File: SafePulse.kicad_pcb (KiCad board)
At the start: 13 copper layers, 40.6 x 20.8 mm, 88 parts, among them IC1 S-35770E01I-K8T2U, J1 Conn_01x03_Male, J2 4208, Q1 FQT7N10L, Q2 BC846A, Q3 MMBT3906, Q4 MMBT3906, U1 TS4061AICT-1.25, U2 74HC14, U3 TLV27L1DBVT, U33 MAX9910EXK+T, U4 CD14538BM

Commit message: Updated production files
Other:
- copper layers 13 -> 4

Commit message: cleaned up files
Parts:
- removed REF**: LOGO, Library:QR_code_SafePulse
- removed U3: TLV27L1DBVT, Package_TO_SOT_SMD:SOT-23-5
- Q2: footprint Package_TO_SOT_SMD:SOT-323_SC-70_Handsoldering -> Package_TO_SOT_SMD:SOT-323_SC-70
- moved C4 2.00 mm to (134.2, 72.9), turned to 180 degrees
- moved H1 1.04 mm to (138.7, 73.0)
- moved C27 0.89 mm to (138.7, 70.2)
- moved R18 0.36 mm to (142.1, 72.7)
- moved R4 0.25 mm to (136.9, 67.7)
- moved C1 0.24 mm to (138.9, 67.7)
- moved C19 0.22 mm to (137.9, 70.4)
- turned U33 to -90 degrees
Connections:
- IC1 pad 7: /SDA -> Net-(IC1-SCL)
- J1 pad 4: Net-(IC1-SDA) -> Net-(IC1-SCL)
- J1 pad 5: /SDA -> Net-(IC1-SDA)
- J2 pad 4: /SDA -> Net-(IC1-SCL)
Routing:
- net /SDA: track 19.7 -> 0.00 mm, vias 2 -> 0
- net Net-(IC1-SCL): track 0.00 -> 16.2 mm, vias 0 -> 2
- net Net-(U33--): track 23.9 -> 15.4 mm
- net Net-(U33-V+): track 21.1 -> 13.1 mm
- net GND: track 64.6 -> 59.6 mm, vias 14 -> 13
- net Net-(U33-+): track 10.0 -> 5.26 mm
- net Net-(R3-Pad2): track 8.62 -> 5.09 mm
- net Net-(C1-Pad1): track 10.2 -> 6.91 mm
- net +3V3: track 51.3 -> 48.2 mm
- net Net-(IC1-SDA): track 18.7 -> 20.3 mm
- net Net-(H1-Pad1): track 5.48 -> 4.25 mm
- net Net-(J1-Pin_1): track 4.55 -> 3.82 mm
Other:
- board text added: "SCL"
- board text added: "SDA"

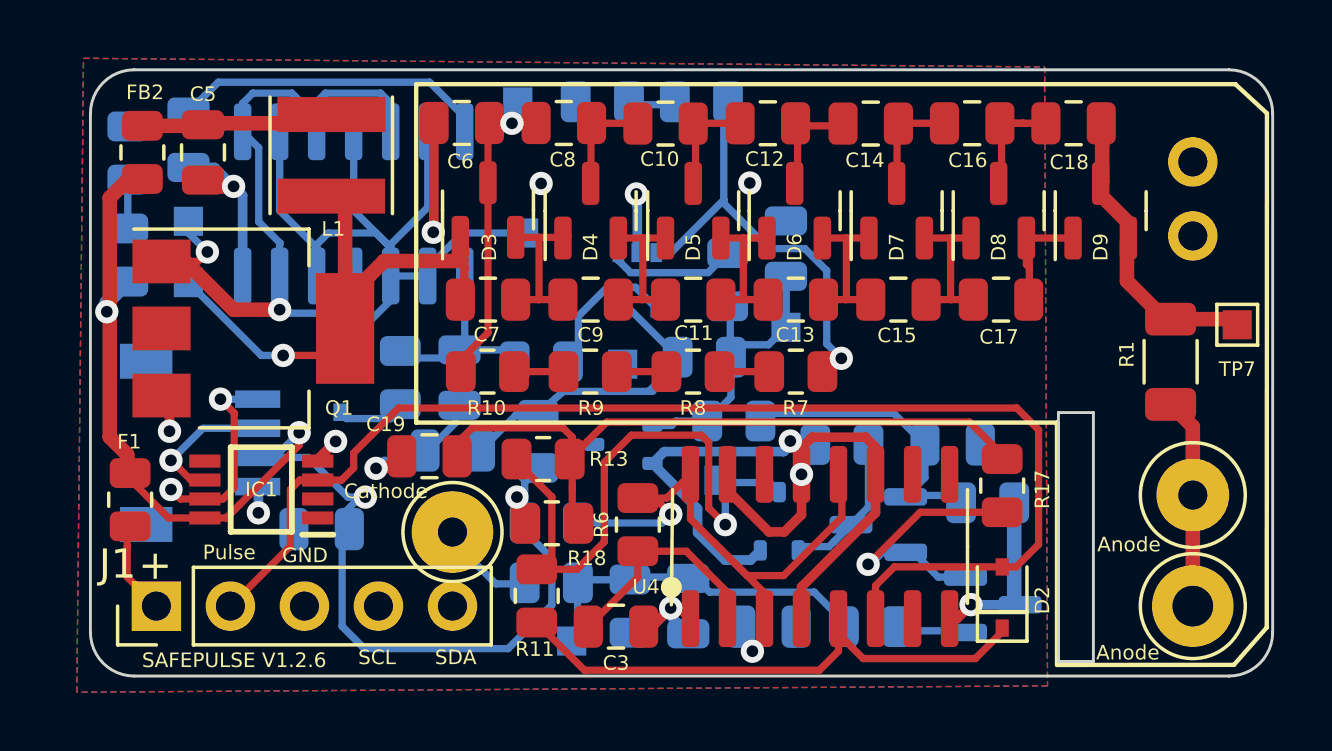
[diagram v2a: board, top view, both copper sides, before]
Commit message: Added QR code and updated files from Allan
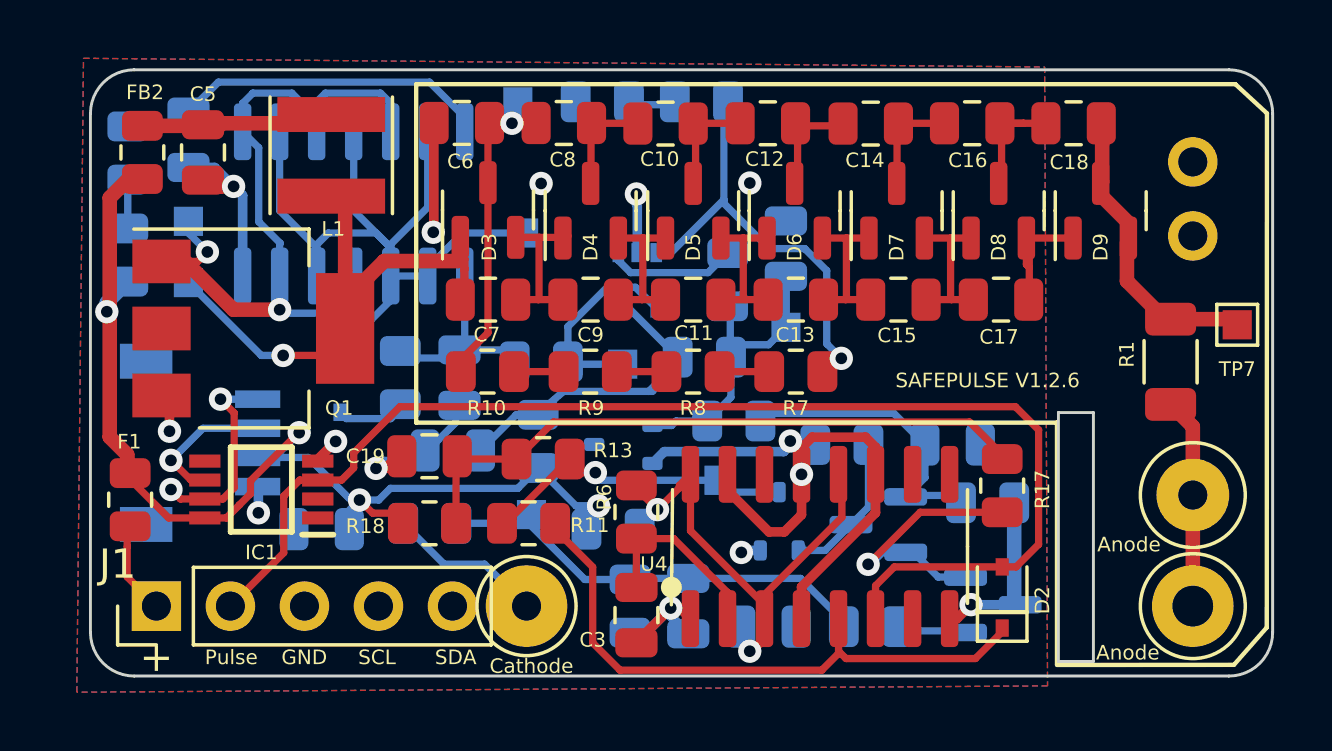
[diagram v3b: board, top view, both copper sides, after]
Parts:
- added REF**: LOGO, Library:QR_code_SafePulse, F.Cu at (156.3, 63.6)
- moved R21 4.64 mm to (137.9, 72.7)
- moved TP8 4.55 mm to (141.4, 72.4)
- moved R18 4.20 mm to (137.9, 72.7)
- moved H1 3.59 mm to (141.2, 75.6)
- moved R11 2.51 mm to (141.3, 72.7), turned to 180 degrees
- moved R12 2.13 mm to (144.2, 72.9)
- moved C3 0.80 mm to (145.0, 75.9), turned to -90 degrees
- moved R6 0.44 mm to (145.0, 72.3)
- turned R13 to 0 degrees
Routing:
- net Net-(Q2-C): track 21.5 -> 11.0 mm
- net +3V3: track 48.2 -> 38.7 mm
- net Net-(U4A-R): track 23.5 -> 17.3 mm
- net GND: track 59.6 -> 54.6 mm, vias 13 -> 14
- net Net-(R3-Pad2): track 5.09 -> 7.32 mm
- net Net-(H1-Pad1): track 4.25 -> 6.11 mm
- net Net-(C22-Pad1): track 13.6 -> 15.2 mm
- net Net-(D2-K): track 19.4 -> 20.9 mm
- net Net-(U4A-RxCx): track 8.55 -> 7.16 mm
- net Net-(C19-Pad1): track 23.7 -> 22.6 mm
- net Net-(Q2-B): track 6.02 -> 5.36 mm
